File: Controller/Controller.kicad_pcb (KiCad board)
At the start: 2 copper layers, 14 x 9 mm, 10 parts, among them SW1 SW_DPST_x2

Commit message: Add sections
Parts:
- PICO-1: moved to B.Cu
- turned PICO-1 to 180 degrees

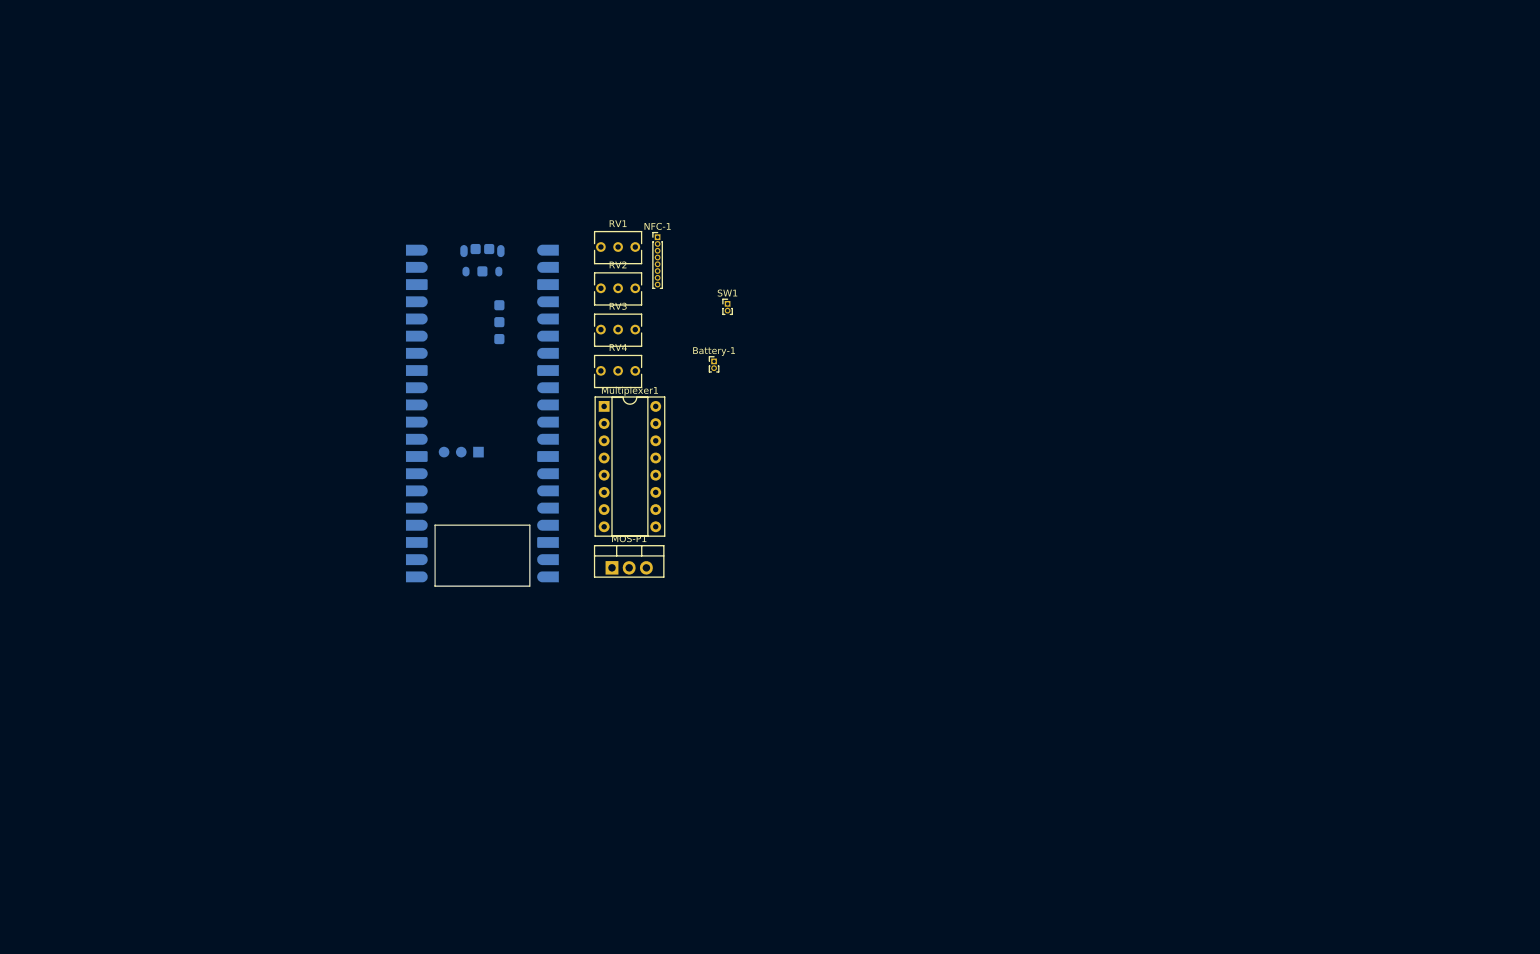
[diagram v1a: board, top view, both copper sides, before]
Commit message: Rewire display
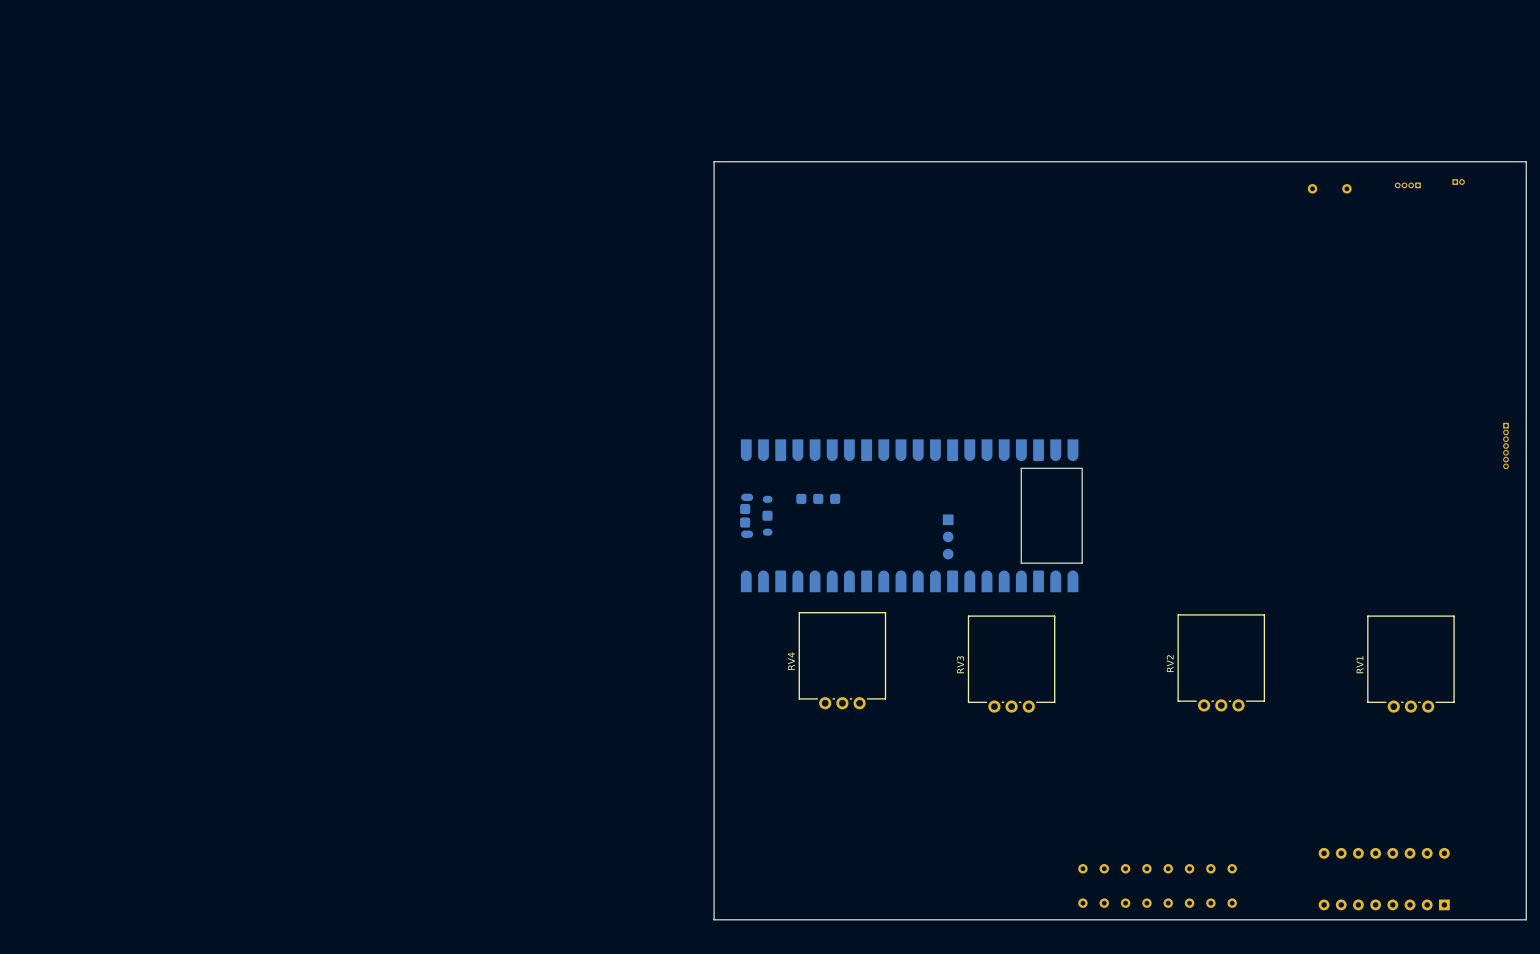
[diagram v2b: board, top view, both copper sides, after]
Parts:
- removed Battery-1: 4x1.2V, Connector_PinHeader_1.00mm:PinHeader_1x02_P1.00mm_Vertical
- removed MOS-P1: FQP27P06, Package_TO_SOT_THT:TO-220-3_Vertical
- removed SW1: SW_DPST_x2, Connector_PinHeader_1.00mm:PinHeader_1x02_P1.00mm_Vertical
- added J1: USB_B, Connector_PinHeader_1.00mm:PinHeader_1x04_P1.00mm_Vertical, B.Cu at (226.0, 40.0)
- added ON/OFF-Switch1: KCD1-101, Connector_PinHeader_1.00mm:PinHeader_1x02_P1.00mm_Vertical, B.Cu at (231.5, 39.5)
- added R-PD-1: ???, Resistor_THT:R_Axial_DIN0204_L3.6mm_D1.6mm_P5.08mm_Horizontal, B.Cu at (215.5, 40.5)
- added R-PU-1: R, Resistor_THT:R_Axial_DIN0204_L3.6mm_D1.6mm_P5.08mm_Horizontal, B.Cu at (176.5, 141.0)
- added R-PU-2: R, Resistor_THT:R_Axial_DIN0204_L3.6mm_D1.6mm_P5.08mm_Horizontal, B.Cu at (179.7, 141.0)
- added R-PU-3: R, Resistor_THT:R_Axial_DIN0204_L3.6mm_D1.6mm_P5.08mm_Horizontal, B.Cu at (182.8, 141.0)
- added R-PU-4: R, Resistor_THT:R_Axial_DIN0204_L3.6mm_D1.6mm_P5.08mm_Horizontal, B.Cu at (185.9, 141.0)
- added R-PU-5: R, Resistor_THT:R_Axial_DIN0204_L3.6mm_D1.6mm_P5.08mm_Horizontal, B.Cu at (189.1, 141.0)
- added R-PU-6: R, Resistor_THT:R_Axial_DIN0204_L3.6mm_D1.6mm_P5.08mm_Horizontal, B.Cu at (192.2, 141.0)
- added R-PU-7: R, Resistor_THT:R_Axial_DIN0204_L3.6mm_D1.6mm_P5.08mm_Horizontal, B.Cu at (195.4, 141.0)
- added R-PU-8: R, Resistor_THT:R_Axial_DIN0204_L3.6mm_D1.6mm_P5.08mm_Horizontal, B.Cu at (198.6, 141.0)
- Multiplexer1: moved to B.Cu
- NFC-1: footprint Connector_PinHeader_1.00mm:PinHeader_1x08_P1.00mm_Vertical -> Connector_PinHeader_1.00mm:PinHeader_1x07_P1.00mm_Vertical; moved to B.Cu
- RV1, RV2, RV3, RV4: footprint Potentiometer_THT:Potentiometer_Bourns_3266Y_Vertical -> Potentiometer_THT:Potentiometer_Vishay_148-149_Single_Vertical
- moved Multiplexer1 144.3 mm to (229.9, 146.3), turned to 90 degrees
- moved RV1 135.4 mm to (227.5, 117.0), turned to 90 degrees
- moved NFC-1 128.4 mm to (239.0, 75.5), turned to 180 degrees
- moved RV2 108.3 mm to (199.5, 116.8), turned to 90 degrees
- moved RV3 80.5 mm to (168.5, 117.0), turned to 90 degrees
- moved PICO-1 64.9 mm to (150.9, 88.8), turned to -90 degrees
- moved RV4 59.2 mm to (143.5, 116.5), turned to 90 degrees
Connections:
- net Net-(Multiplexer1-A) renamed POTS
- Multiplexer1 pad 1: unconnected-(Multiplexer1-A4-Pad1) -> GND
- Multiplexer1 pad 2: unconnected-(Multiplexer1-A6-Pad2) -> GND
- Multiplexer1 pad 4: unconnected-(Multiplexer1-A7-Pad4) -> GND
- Multiplexer1 pad 5: unconnected-(Multiplexer1-A5-Pad5) -> GND
- Multiplexer1 pad 6: unconnected-(Multiplexer1-~{E}-Pad6) -> GND
- NFC-1 pad 2: Net-(NFC-1-RST) -> GP22
- PICO-1 pad 10: unconnected-(PICO-1-I2C1_SCL/SPI0_TX/GP7-Pad10) -> Net-(Multiplexer1-S0)
- PICO-1 pad 11: unconnected-(PICO-1-UART1_TX/I2C0_SDA/SPI1_RX/GP8-Pad11) -> Net-(DISPLAY1-LCD_DC)
- PICO-1 pad 12: unconnected-(PICO-1-UART1_RX/I2C0_SCL/SPI1_CSN/GP9-Pad12) -> Net-(DISPLAY1-LCD_CS)
- PICO-1 pad 14: Net-(Multiplexer1-S2) -> Net-(DISPLAY1-LCD_SCLK)
- PICO-1 pad 15: Net-(Multiplexer1-S1) -> Net-(DISPLAY1-LCD_MOSI)
- PICO-1 pad 16: Net-(Multiplexer1-S0) -> LED
- PICO-1 pad 17: unconnected-(PICO-1-UART0_RX/I2C0_SCL/SPI1_CSN/GP13-Pad17) -> Net-(PICO-1-UART0_RX/I2C0_SCL/SPI1_CSN/GP13)
- PICO-1 pad 19: unconnected-(PICO-1-I2C1_SDA/SPI1_SCK/GP14-Pad19) -> Net-(PICO-1-I2C1_SDA/SPI1_SCK/GP14)
- PICO-1 pad 20: unconnected-(PICO-1-I2C1_SCL/SPI1_TX/GP15-Pad20) -> Net-(PICO-1-I2C1_SCL/SPI1_TX/GP15)
- PICO-1 pad 21: unconnected-(PICO-1-UART0_TX/I2C0_SDA/SPI0_RX/GP16-Pad21) -> Net-(PICO-1-UART0_TX/I2C0_SDA/SPI0_RX/GP16)
- PICO-1 pad 22: unconnected-(PICO-1-UART0_RX/I2C0_SCL/SPI0_CSN/GP17-Pad22) -> Net-(PICO-1-UART0_RX/I2C0_SCL/SPI0_CSN/GP17)
- PICO-1 pad 24: unconnected-(PICO-1-I2C1_SDA/SPI0_SCK/GP18-Pad24) -> Net-(PICO-1-I2C1_SDA/SPI0_SCK/GP18)
- PICO-1 pad 25: unconnected-(PICO-1-I2C1_SCL/SPI0_TX/GP19-Pad25) -> Net-(PICO-1-I2C1_SCL/SPI0_TX/GP19)
- PICO-1 pad 26: unconnected-(PICO-1-I2C0_SDA/GP20-Pad26) -> Net-(PICO-1-I2C0_SDA/GP20)
- PICO-1 pad 27: unconnected-(PICO-1-12C0_SCL/GP21-Pad27) -> GP21
- PICO-1 pad 29: unconnected-(PICO-1-GP22-Pad29) -> GP22
- PICO-1 pad 30: Net-(NFC-1-RST) -> Net-(DISPLAY1-RESET)
- PICO-1 pad 32: unconnected-(PICO-1-I2C1_SCL/ADC1/GP27-Pad32) -> GP27
- PICO-1 pad 6: unconnected-(PICO-1-UART1_TX/I2C0_SDA/SPI0_RX/GP4-Pad6) -> Net-(DISPLAY1-BACKLIGHT_EN)
- PICO-1 pad 7: unconnected-(PICO-1-UART1_RX/I2C0_SCL/SPI0_CSN/GP5-Pad7) -> Net-(Multiplexer1-S2)
- PICO-1 pad 9: unconnected-(PICO-1-I2C1_SDA/SPI0_SCK/GP6-Pad9) -> Net-(Multiplexer1-S1)
- PICO-1 pad A: Net-(PICO-1-USB_SHIELD-PadA) -> unconnected-(PICO-1-USB_SHIELD-PadA)_3
- PICO-1 pad B: Net-(PICO-1-USB_SHIELD-PadA) -> unconnected-(PICO-1-USB_SHIELD-PadA)_2
- PICO-1 pad C: Net-(PICO-1-USB_SHIELD-PadA) -> unconnected-(PICO-1-USB_SHIELD-PadA)_1
- PICO-1 pad D: Net-(PICO-1-USB_SHIELD-PadA) -> unconnected-(PICO-1-USB_SHIELD-PadA)
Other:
- board size 14 x 9 mm -> 120 x 112 mm

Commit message: Add components and lign up PCB
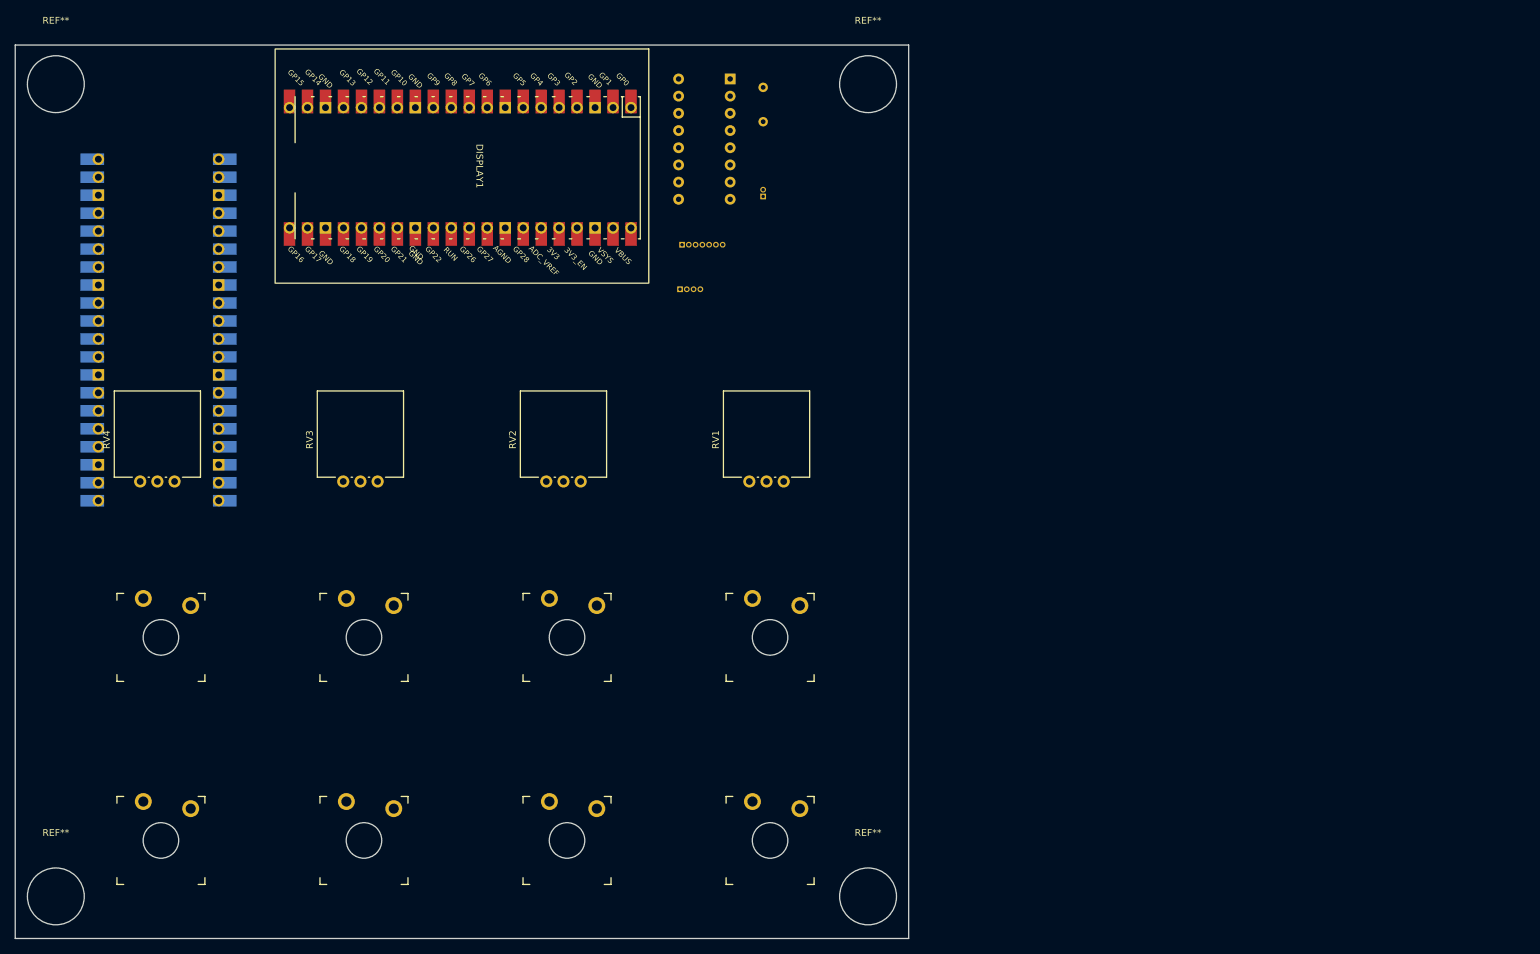
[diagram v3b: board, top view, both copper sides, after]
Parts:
- removed R-PU-1, R-PU-2, R-PU-3, R-PU-4, R-PU-5, R-PU-6, R-PU-7, R-PU-8: R, Resistor_THT:R_Axial_DIN0204_L3.6mm_D1.6mm_P5.08mm_Horizontal
- added DISPLAY1: ~, PIM580:display-footprint, F.Cu at (86.8, 37.1)
- added REF**: MountingHole_8.4mm_M8, MountingHole:MountingHole_8.4mm_M8, F.Cu at (144.8, 25.0)
- added REF**: MountingHole_8.4mm_M8, MountingHole:MountingHole_8.4mm_M8, F.Cu at (24.8, 25.0)
- added REF**: MountingHole_8.4mm_M8, MountingHole:MountingHole_8.4mm_M8, F.Cu at (24.8, 145.0)
- added REF**: MountingHole_8.4mm_M8, MountingHole:MountingHole_8.4mm_M8, F.Cu at (144.8, 145.0)
- added SW2: SW_Push, Gateron:SW_Gateron_LowProfile_HotSwap_THT (1), F.Cu at (40.3, 106.8)
- added SW3: SW_Push, Gateron:SW_Gateron_LowProfile_HotSwap_THT (1), F.Cu at (40.3, 136.8)
- added SW4: SW_Push, Gateron:SW_Gateron_LowProfile_HotSwap_THT (1), F.Cu at (70.3, 106.8)
- added SW5: SW_Push, Gateron:SW_Gateron_LowProfile_HotSwap_THT (1), F.Cu at (70.3, 136.8)
- added SW6: SW_Push, Gateron:SW_Gateron_LowProfile_HotSwap_THT (1), F.Cu at (100.3, 106.8)
- added SW7: SW_Push, Gateron:SW_Gateron_LowProfile_HotSwap_THT (1), F.Cu at (100.3, 136.8)
- added SW8: SW_Push, Gateron:SW_Gateron_LowProfile_HotSwap_THT (1), F.Cu at (130.3, 106.8)
- added SW9: SW_Push, Gateron:SW_Gateron_LowProfile_HotSwap_THT (1), F.Cu at (130.3, 136.8)
- PICO-1: footprint RASPBERRY_PI_PICO_W:MODULE_RASPBERRY_PI_PICO_W -> RASPBERRY_PI_PICO_W:pico-footprint
- moved Multiplexer1 161.3 mm to (124.4, 24.3), turned to 180 degrees
- moved NFC-1 124.6 mm to (117.3, 48.8), turned to -90 degrees
- moved PICO-1 114.1 mm to (39.9, 62.4), turned to 0 degrees
- moved J1 110.1 mm to (117.0, 55.3), turned to -90 degrees
- moved RV4 106.4 mm to (42.3, 83.7)
- moved RV2 102.7 mm to (102.3, 83.7)
- moved ON/OFF-Switch1 102.3 mm to (129.2, 41.6), turned to 0 degrees
- moved RV3 101.8 mm to (72.3, 83.7)
- moved RV1 100.9 mm to (132.3, 83.7)
- moved R-PD-1 87.5 mm to (129.2, 25.5), turned to -90 degrees
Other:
- board size 120 x 112 mm -> 132 x 132 mm

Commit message: PCB Routing
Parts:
- removed R-PD-1: ???, Resistor_THT:R_Axial_DIN0204_L3.6mm_D1.6mm_P5.08mm_Horizontal
- added LDR_R1: ???, Resistor_THT:R_Axial_DIN0204_L3.6mm_D1.6mm_P5.08mm_Horizontal, B.Cu at (119.2, 32.0)
- added R2: LDR03, Connector_PinHeader_1.00mm:PinHeader_1x02_P1.00mm_Vertical, B.Cu at (124.4, 36.8)
- moved Multiplexer1 58.3 mm to (76.2, 57.1), turned to -90 degrees
- moved J1 30.8 mm to (116.2, 24.5)
- moved NFC-1 19.8 mm to (124.4, 30.3)
- moved ON/OFF-Switch1 17.2 mm to (130.4, 24.5), turned to 90 degrees
- moved PICO-1 3.82 mm to (39.9, 66.3), turned to 180 degrees
- moved RV1 3.00 mm to (132.3, 80.7)
- moved RV2 3.00 mm to (102.3, 80.7)
- moved RV3 3.00 mm to (72.3, 80.7)
- moved RV4 3.00 mm to (42.3, 80.7)
- moved SW4 0.53 mm to (69.8, 106.8)
- moved SW5 0.53 mm to (69.8, 136.8)
- moved SW6 0.53 mm to (99.8, 106.8)
- moved SW7 0.53 mm to (99.8, 136.8)
- moved SW8 0.53 mm to (129.8, 106.8)
- moved SW9 0.53 mm to (129.8, 136.8)
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- renumbered REF** to HOLE_1, REF** to HOLE_2, REF** to HOLE_3, REF** to HOLE_4
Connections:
- Multiplexer1 pad 1: GND -> Net-(Multiplexer1-A4)
- ON/OFF-Switch1 pad 1: (no net) -> Net-(J1-VBUS)
- ON/OFF-Switch1 pad 2: (no net) -> +5V
- PICO-1 pad 39: Net-(MOS-P1-S) -> +5V
- PICO-1 pad 40: Net-(MOS-P1-G) -> unconnected-(PICO-1-VBUS-Pad40)
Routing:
- net GND: track 0.00 -> 343.3 mm, vias 0 -> 2
- net 3V3: track 0.00 -> 230.8 mm, vias 0 -> 1
- net Net-(SW2-Pad2): track 0.00 -> 212.0 mm
- net GP22: track 0.00 -> 134.7 mm, vias 0 -> 1
- net Net-(PICO-1-I2C0_SDA/GP20): track 0.00 -> 133.4 mm, vias 0 -> 1
- net GP21: track 0.00 -> 131.0 mm, vias 0 -> 2
- net GP27: track 0.00 -> 129.5 mm, vias 0 -> 1
- net Net-(PICO-1-I2C1_SDA/SPI0_SCK/GP18): track 0.00 -> 108.7 mm, vias 0 -> 1
- net +5V: track 0.00 -> 106.8 mm
- net Net-(PICO-1-I2C1_SCL/SPI0_TX/GP19): track 0.00 -> 104.1 mm
- net Net-(NFC-1-MOSI): track 0.00 -> 96.0 mm
- net Net-(NFC-1-SCK): track 0.00 -> 94.1 mm
- net Net-(NFC-1-MISO/SCL/TX): track 0.00 -> 85.0 mm
- net Net-(DISPLAY1-RESET): track 0.00 -> 79.4 mm, vias 0 -> 2
- net Net-(PICO-1-UART0_TX/I2C0_SDA/SPI0_RX/GP16): track 0.00 -> 73.1 mm, vias 0 -> 1
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- added copper zone on B.Cu, net GND
- added copper zone on F.Cu, net GND
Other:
- board text added: "ETIMC Controller v1 De Danske Geder SpilTek 2022"

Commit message: Update PCB
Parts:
- J1: footprint Connector_PinHeader_1.00mm:PinHeader_1x04_P1.00mm_Vertical -> Connector_PinHeader_2.54mm:PinHeader_1x04_P2.54mm_Vertical
- NFC-1: footprint Connector_PinHeader_1.00mm:PinHeader_1x07_P1.00mm_Vertical -> Connector_PinHeader_2.54mm:PinHeader_1x07_P2.54mm_Vertical
- ON/OFF-Switch1, R2: footprint Connector_PinHeader_1.00mm:PinHeader_1x02_P1.00mm_Vertical -> Connector_PinHeader_2.54mm:PinHeader_1x02_P2.54mm_Vertical
- moved NFC-1 9.27 mm to (115.2, 29.7)
- moved LDR_R1 5.25 mm to (114.4, 34.1)
- moved R2 3.92 mm to (127.8, 35.0)
- moved J1 1.08 mm to (115.2, 24.5)
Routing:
- net GND: track 343.3 -> 0.00 mm, vias 2 -> 0
- net Net-(Multiplexer1-A0): track 52.2 -> 71.7 mm, vias 1 -> 0
- net 3V3: track 230.8 -> 247.0 mm, vias 1 -> 0
- net Net-(DISPLAY1-RESET): track 79.4 -> 64.3 mm, vias 2 -> 1
- net Net-(Multiplexer1-A2): track 44.5 -> 32.2 mm, vias 1 -> 0
- net Net-(Multiplexer1-A3): track 62.3 -> 50.2 mm, vias 1 -> 0
- net Net-(NFC-1-MOSI): track 96.0 -> 107.1 mm, vias 0 -> 1
- net Net-(DISPLAY1-LCD_MOSI): track 50.4 -> 43.6 mm, vias 1 -> 0
- net Net-(PICO-1-UART0_RX/I2C0_SCL/SPI1_CSN/GP13): track 27.3 -> 21.9 mm, vias 1 -> 0
- net GP27: track 129.5 -> 124.4 mm
- net Net-(PICO-1-I2C1_SDA/SPI0_SCK/GP18): track 108.7 -> 104.0 mm
- net Net-(PICO-1-I2C1_SCL/SPI1_TX/GP15): track 26.1 -> 21.9 mm, vias 1 -> 0
- net Net-(PICO-1-I2C0_SDA/GP20): track 133.4 -> 137.6 mm
- net GP22: track 134.7 -> 130.6 mm
- net GP21: track 131.0 -> 134.8 mm, vias 2 -> 1
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
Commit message: Fix the pcb
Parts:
- moved NFC-1 76.9 mm to (38.5, 24.5)
- moved J1 10.5 mm to (115.5, 35.0), turned to 0 degrees
- moved LDR_R1 6.60 mm to (121.0, 34.1)
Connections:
- J1 pad 2: GP27 -> GP20
- PICO-1 pad 26: Net-(PICO-1-I2C0_SDA/GP20) -> GP20
- PICO-1 pad 32: GP27 -> Net-(PICO-1-I2C1_SCL/ADC1/GP27)
- SW9 pad 1: Net-(PICO-1-I2C0_SDA/GP20) -> Net-(PICO-1-I2C1_SCL/ADC1/GP27)
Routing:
- net GND: track 0.00 -> 640.1 mm, vias 0 -> 3
- net 3V3: track 247.0 -> 491.9 mm, vias 0 -> 2
- net Net-(PICO-1-I2C1_SCL/ADC1/GP27): track 0.00 -> 164.8 mm, vias 0 -> 1
- net Net-(PICO-1-I2C0_SDA/GP20): track 137.6 -> 0.00 mm, vias 1 -> 0
- net GP27: track 124.4 -> 0.00 mm, vias 1 -> 0
- net GP20: track 0.00 -> 110.5 mm
- net GP22: track 130.6 -> 57.1 mm, vias 1 -> 0
- net Net-(NFC-1-MOSI): track 107.1 -> 35.8 mm, vias 1 -> 0
- net Net-(NFC-1-MISO/SCL/TX): track 82.0 -> 17.7 mm
- net Net-(NFC-1-SCK): track 95.2 -> 39.2 mm
- net POTS: track 55.5 -> 100.1 mm, vias 1 -> 0
- net Net-(DISPLAY1-RESET): track 64.3 -> 105.6 mm
- net Net-(DISPLAY1-LCD_MOSI): track 43.6 -> 80.3 mm, vias 0 -> 1
- net Net-(PICO-1-UART0_RX/I2C0_SCL/SPI0_CSN/GP17): track 70.8 -> 106.8 mm, vias 0 -> 1
- net Net-(DISPLAY1-LCD_CS): track 32.3 -> 59.1 mm, vias 0 -> 1
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- removed copper zone on B.Cu, net GND
- removed copper zone on F.Cu, net GND

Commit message: Export gerber
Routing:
- net Net-(Multiplexer1-A4): track 71.0 -> 64.8 mm
- net 3V3: track 491.9 -> 489.9 mm
- added copper zone on B.Cu, net GND
- added copper zone on F.Cu, net GND
